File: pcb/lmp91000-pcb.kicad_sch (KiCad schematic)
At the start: 17 parts, among them J1 TC2030, U1 2450AT18D0100001E, U2 EFR32BG24L210F768IM40-B, Y1 XTL501250-S315-038

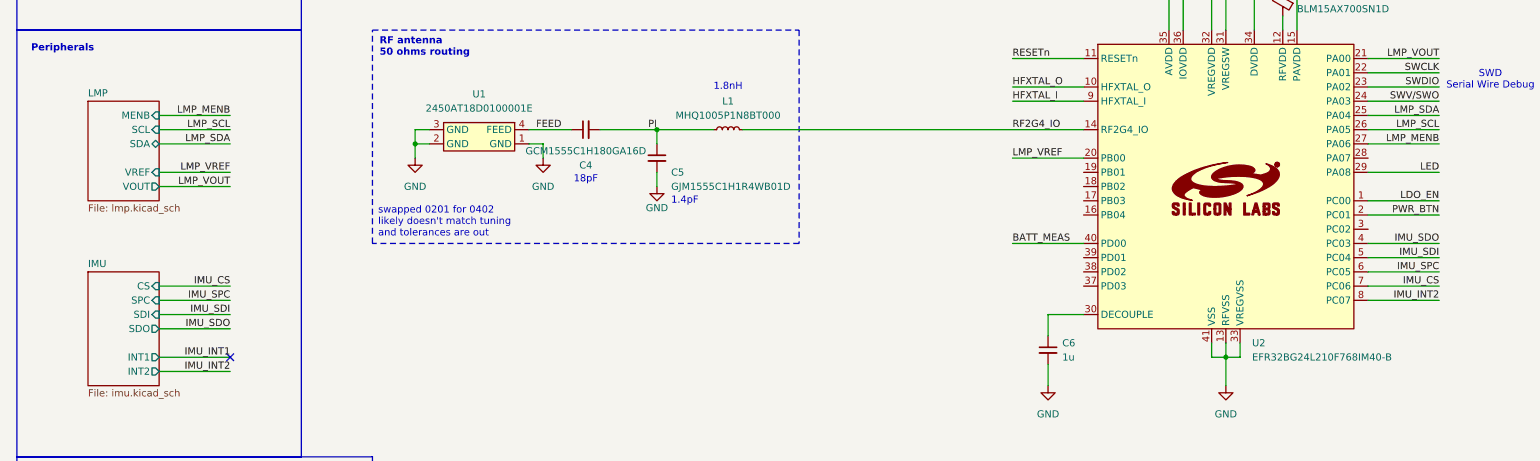
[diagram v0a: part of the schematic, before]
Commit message: add c1 and int1 to pcb
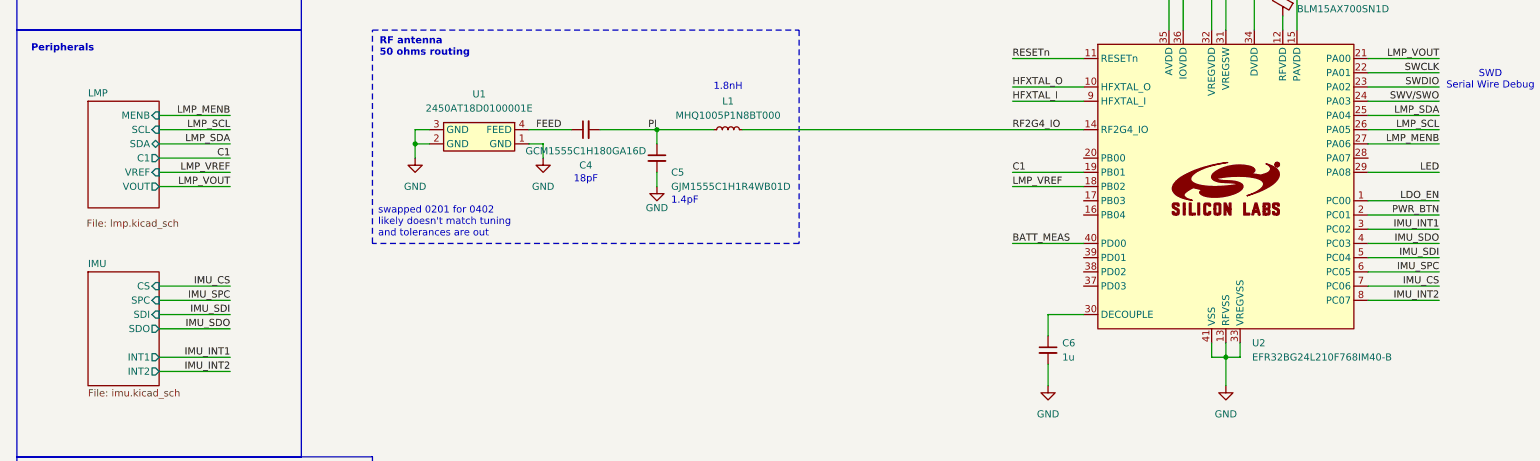
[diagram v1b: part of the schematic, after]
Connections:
- net IMU_INT1: now also U2.3 (PC02)
- net LMP_VREF: now also U2.18 (PB02); no longer U2.20 (PB00)
- net C1: now reaches U2.19 (PB01)
- no-connect marks 1 -> 0
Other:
- sheet LMP ports: added C1; removed none

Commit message: Redesign for board order. add LFXO and shield electrode traces better
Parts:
- added Y2: KDS-DST1610A, crystal_smd_dst1610a:KDS-DST1610A, symbol Device:Crystal
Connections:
- net BATT_MEAS: now also U2.29 (PA08); no longer U2.40 (PD00)
- net LED: now also U2.28 (PA07); no longer U2.29 (PA08)
- net LFXTAL_I: now reaches U2.39 (PD01)
- net LFXTAL_I: now also Y2.1
- new net LFXTAL_O: U2.40 (PD00), Y2.2
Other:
- note added: "32.768KHz for internal RTC"
- note added: "LF Crystal"
